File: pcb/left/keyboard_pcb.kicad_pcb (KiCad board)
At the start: 2 copper layers, 138.8 x 89.9 mm, 52 parts, among them J1 TRRS, K0 KEYSW, K1 KEYSW, K10 KEYSW, K11 KEYSW, K12 KEYSW, K13 KEYSW, K14 KEYSW, K15 KEYSW, K2 KEYSW, K20 KEYSW, K21 KEYSW, K22 KEYSW, K23 KEYSW, K24 KEYSW, K25 KEYSW, K3 KEYSW, K30 KEYSW, K31 KEYSW, K32 KEYSW, K4 KEYSW, K5 KEYSW, U1 MCP23009-E/SO, U2 Pico, U3 PCF8574TS

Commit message: Left side routing wip
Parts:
- removed U3: PCF8574TS, Package_SO:SSOP-20_4.4x6.5mm_P0.65mm
- R10, R11, R12, R13, R5, R8, R9, TP1: moved to B.Cu
- moved TP1 224.8 mm to (208.2, 91.5), turned to 180 degrees
- moved R5 87.9 mm to (184.8, 65.5)
- moved R10 87.5 mm to (186.5, 88.8), turned to 0 degrees
- moved R9 83.0 mm to (186.5, 92.2), turned to 0 degrees
- moved R8 81.0 mm to (186.5, 94.0), turned to 0 degrees
- moved R11 79.1 mm to (186.5, 95.8), turned to 0 degrees
- moved C1 73.6 mm to (191.2, 59.0), turned to 90 degrees
- moved C2 73.1 mm to (189.8, 59.0), turned to 90 degrees
- moved R12 62.4 mm to (186.5, 90.5), turned to 0 degrees
- moved R13 42.1 mm to (186.5, 87.0)
- moved R14 6.68 mm to (185.8, 82.2), turned to 0 degrees
- moved R4 3.87 mm to (184.8, 59.2)
- moved U1 3.77 mm to (189.8, 73.8)
- moved R3 0.50 mm to (184.8, 61.0)
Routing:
- net +3.3V: track 194.4 -> 0.00 mm, vias 8 -> 0
- net /k20: track 40.1 -> 162.9 mm, vias 0 -> 1
- net /LED_A: track 9.34 -> 118.1 mm, vias 0 -> 1
- net /LED_B: track 11.1 -> 95.8 mm, vias 0 -> 1
- net /k30: track 19.3 -> 99.2 mm, vias 0 -> 1
- net /k31: track 20.3 -> 76.1 mm, vias 0 -> 1
- net /k32: track 24.4 -> 72.9 mm, vias 0 -> 1
- net /SDA: track 30.4 -> 0.00 mm, vias 3 -> 0
- net /SCL: track 27.2 -> 0.00 mm, vias 3 -> 0
- net GND: track 114.5 -> 93.5 mm, vias 51 -> 42
- net /I2C_Int: track 93.0 -> 77.2 mm
- net VCC: track 50.7 -> 65.5 mm
- net /k10: track 69.9 -> 61.0 mm
- net /k00: track 78.4 -> 74.5 mm
- net tx: track 71.5 -> 74.2 mm
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
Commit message: Rev 1.1 WIP
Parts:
- R6, R7: moved to B.Cu
- TP1, U1: moved to F.Cu
- moved TP1 94.6 mm to (114.8, 105.8), turned to 0 degrees
- moved C1 79.3 mm to (129.9, 109.2), turned to -90 degrees
- moved C2 76.6 mm to (131.9, 109.2), turned to -90 degrees
- moved R4 74.7 mm to (126.1, 105.5), turned to 90 degrees
- moved R5 74.2 mm to (122.2, 105.5), turned to 90 degrees
- moved U1 73.2 mm to (124.8, 107.7), turned to -90 degrees
- moved R3 72.1 mm to (128.0, 105.5), turned to 90 degrees
- moved R10 71.2 mm to (118.3, 109.2), turned to -90 degrees
- moved R13 69.9 mm to (120.2, 109.2), turned to -90 degrees
- moved R9 69.5 mm to (118.3, 105.5), turned to 90 degrees
- moved R8 67.2 mm to (120.3, 105.5), turned to 90 degrees
- moved R12 67.0 mm to (122.2, 109.2), turned to -90 degrees
- moved R14 65.9 mm to (124.1, 105.5), turned to 90 degrees
- moved R11 63.8 mm to (124.1, 109.2), turned to -90 degrees
- moved R6 20.8 mm to (126.1, 109.2), turned to 90 degrees
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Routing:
- net +3.3V: track 0.00 -> 139.9 mm, vias 0 -> 6
- net /SDA: track 0.00 -> 116.0 mm, vias 0 -> 1
- net /LED_A: track 118.1 -> 6.64 mm
- net /SCL: track 0.00 -> 109.6 mm, vias 0 -> 1
- net /k20: track 162.9 -> 73.2 mm, vias 1 -> 2
- net /LED_B: track 95.8 -> 6.92 mm
- net /k30: track 99.2 -> 38.0 mm
- net /k00: track 74.5 -> 103.3 mm, vias 0 -> 1
- net GND: track 93.5 -> 121.0 mm, vias 42 -> 45
- net Net-(D1-A): track 0.00 -> 24.2 mm, vias 0 -> 1
- net /k32: track 72.9 -> 95.4 mm
- net /k10: track 61.0 -> 78.4 mm, vias 0 -> 1
- net /MCP_RST: track 0.00 -> 16.9 mm, vias 0 -> 1
- net /I2C_Int: track 77.2 -> 91.9 mm, vias 0 -> 2
- net Net-(D2-A): track 2.31 -> 15.9 mm, vias 0 -> 1
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
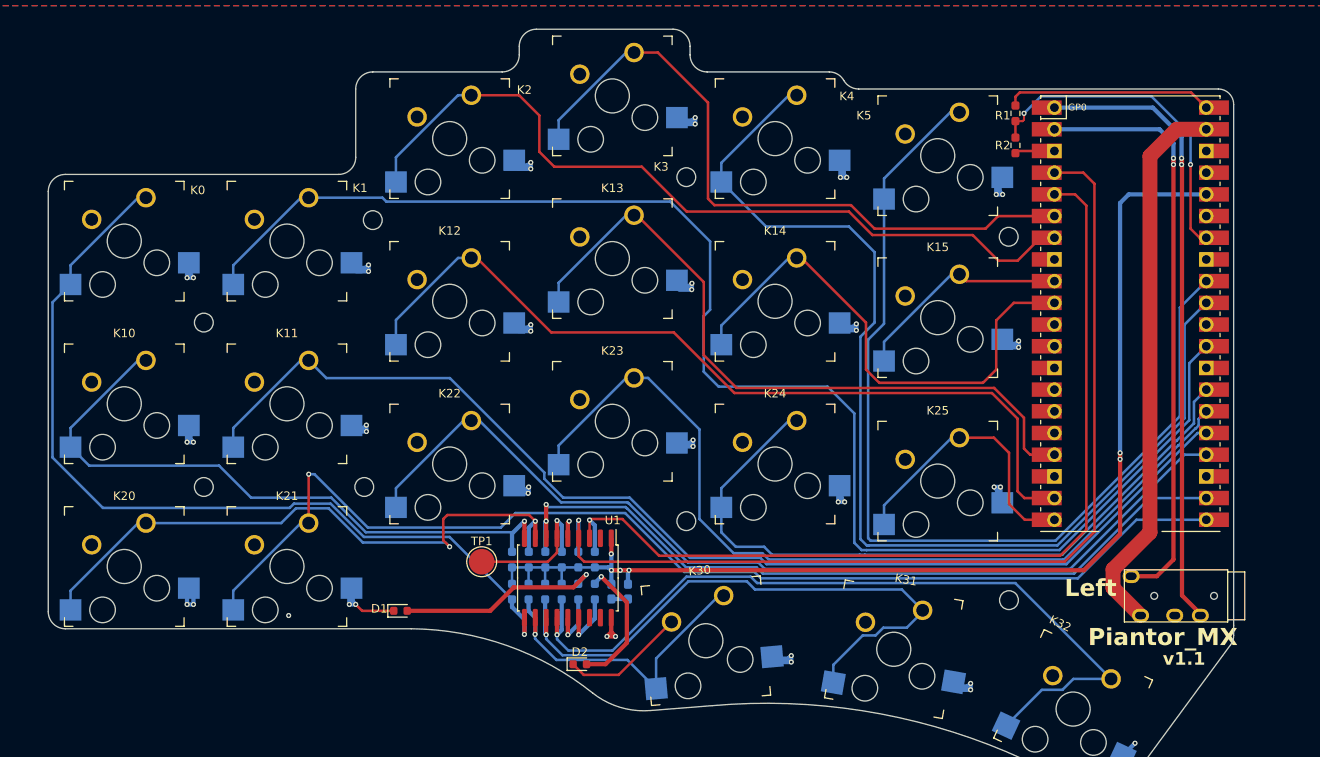
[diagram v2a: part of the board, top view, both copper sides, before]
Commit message: Revision 1.1 -RFR- new standoff holes added and left/right pcb positions synced
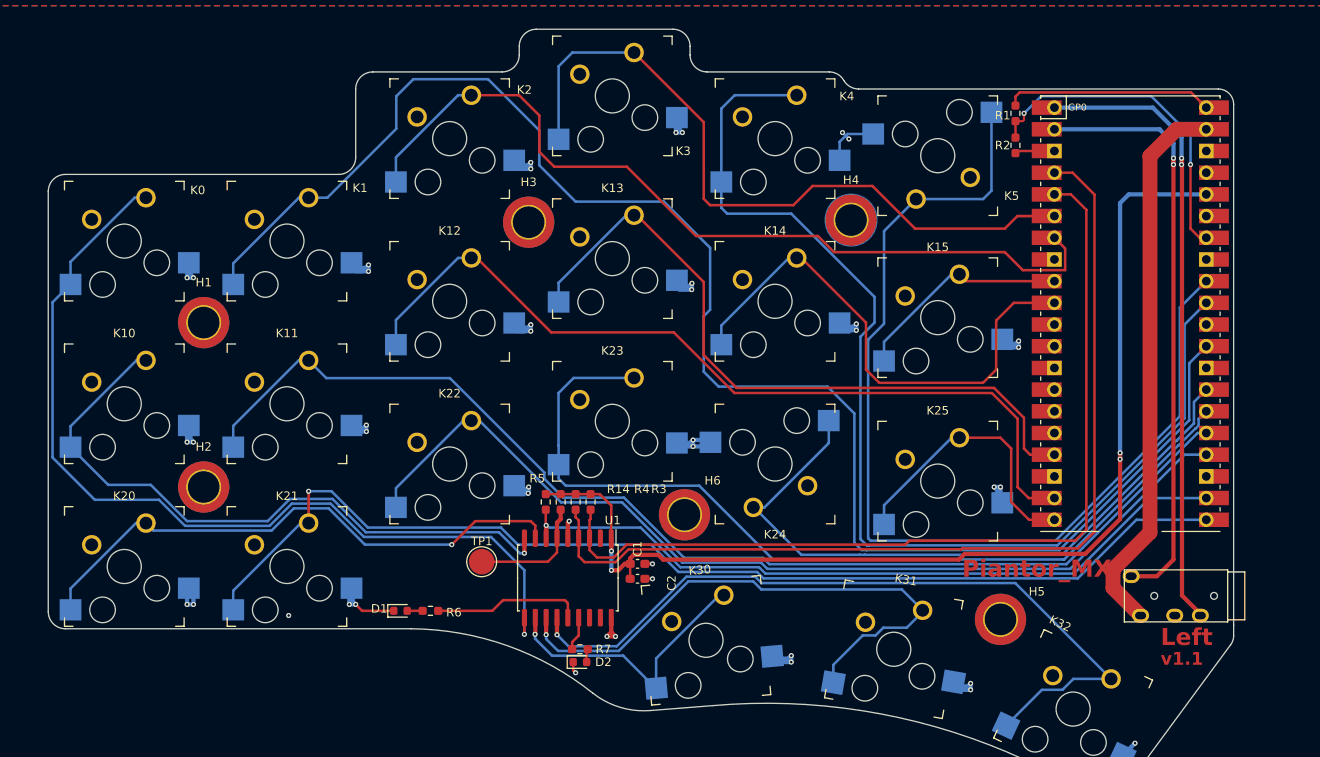
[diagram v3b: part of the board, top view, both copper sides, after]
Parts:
- removed H7, H8: MountingHole, misc:MountingHole_2.2mm_M2-8mm
- removed R10, R11, R12, R13, R8, R9: 10k, Resistor_SMD:R_0603_1608Metric_Pad0.98x0.95mm_HandSolder
- C1, C2, R14, R3, R4, R5, R6, R7: moved to F.Cu
- H1, H2, H3, H4, H5, H6: footprint misc:MountingHole_2.2mm_M2-8mm -> misc:MountingHole_3.7mm_Pad_TopBottom
- moved H2 37.0 mm to (82.2, 97.0)
- moved H3 19.2 mm to (120.2, 66.0)
- moved H4 18.6 mm to (158.0, 65.8)
- moved R6 17.5 mm to (108.8, 111.5), turned to 180 degrees
- moved R7 6.97 mm to (126.2, 116.0), turned to 0 degrees
- moved R3 6.77 mm to (127.5, 98.8), turned to -90 degrees
- moved R4 6.76 mm to (125.8, 98.8), turned to -90 degrees
- moved R14 6.75 mm to (124.0, 98.8), turned to -90 degrees
- moved R5 6.75 mm to (122.2, 98.8), turned to -90 degrees
- moved C1 4.46 mm to (133.0, 106.0), turned to 0 degrees
- moved H5 2.46 mm to (175.5, 112.5)
- moved C2 1.87 mm to (133.0, 107.8), turned to 0 degrees
- moved H6 0.78 mm to (138.5, 100.2)
- moved D2 0.25 mm to (126.2, 117.5)
- moved K30 0.05 mm to (141.0, 114.9)
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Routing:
- net Net-(D1-A): track 24.2 -> 1.81 mm, vias 1 -> 0
- net /k01: track 169.2 -> 185.0 mm
- net Net-(D2-A): track 15.9 -> 1.81 mm, vias 1 -> 0
- net GND: track 121.0 -> 107.6 mm, vias 45 -> 44
- net +3.3V: track 139.9 -> 128.8 mm, vias 6 -> 4
- net /LED_A: track 6.64 -> 17.5 mm, vias 1 -> 0
- net /k20: track 73.2 -> 66.1 mm, vias 2 -> 1
- net /k05: track 114.7 -> 120.2 mm
- net /I2C_Int: track 91.9 -> 86.6 mm, vias 2 -> 1
- net /k32: track 95.4 -> 90.3 mm
- net /k24: track 84.6 -> 79.6 mm
- net /k02: track 94.6 -> 99.5 mm
- net /k00: track 103.3 -> 108.1 mm
- net /k31: track 71.8 -> 67.2 mm
- net /k30: track 38.0 -> 33.6 mm
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
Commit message: Revision 1.1 -RFR- right pcb layout fix added Standoff PN
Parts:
- R6, R7: value R -> 1k
